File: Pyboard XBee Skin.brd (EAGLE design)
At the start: 33 x 26.9 mm, 8 parts

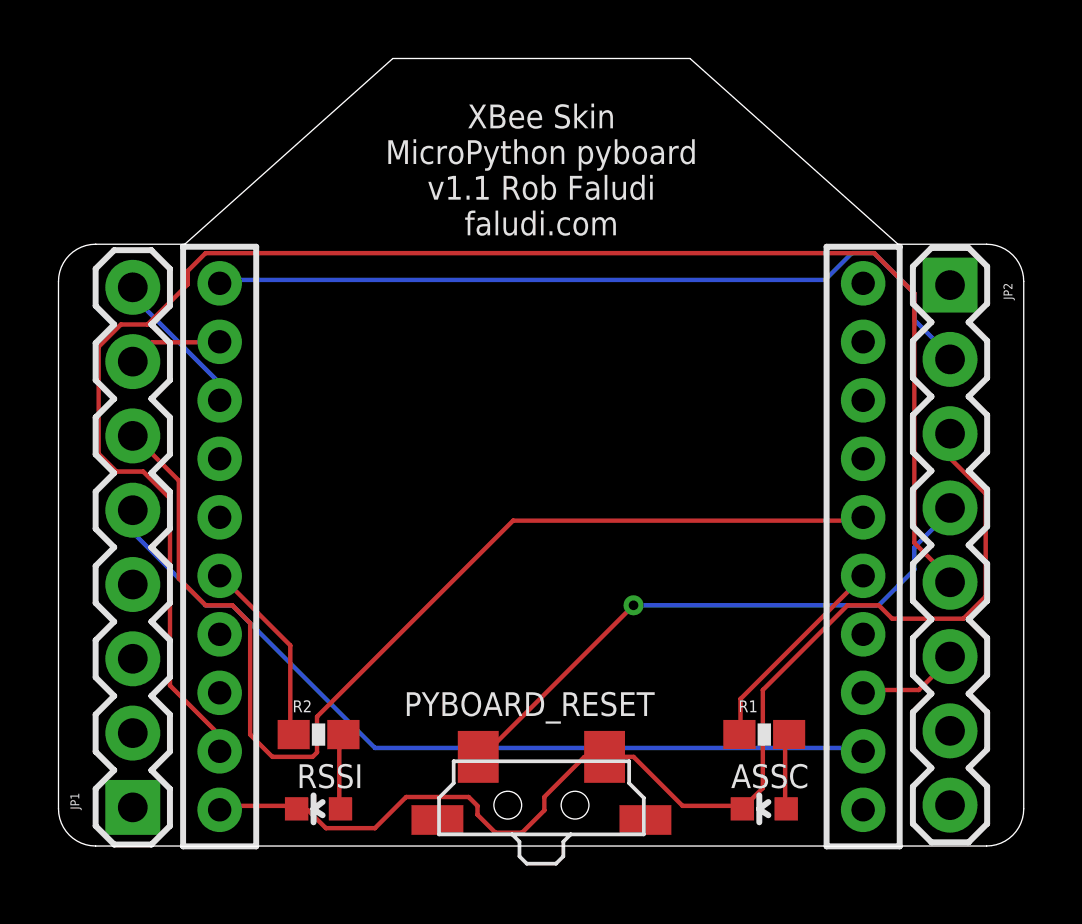
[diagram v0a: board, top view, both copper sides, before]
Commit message: Eagle CAD board design file v1.2
updates to silkscreen and reposition reset button
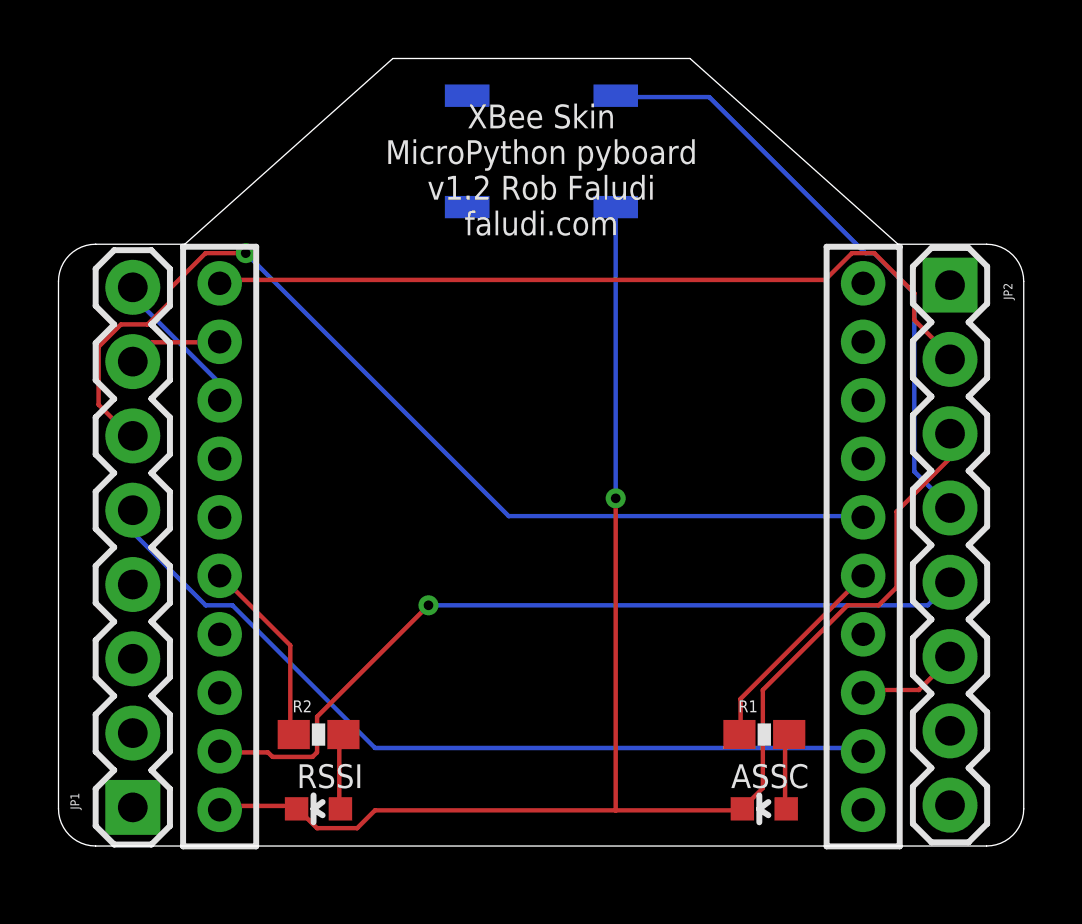
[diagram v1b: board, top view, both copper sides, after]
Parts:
- PYBOARD_RESET: device Seeed-OPL-Button:SW4-SMD-7.0X3.5X3.5MM-90D -> SparkFun-Electromechanical:TACTILE_SWITCH_SMD
- moved PYBOARD_RESET 22.4 mm to (16.5, 23.7), flipped to the bottom
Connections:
- net GND: now also PYBOARD_RESET.3; no longer PYBOARD_RESET.2
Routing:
- net SLP_CTRL: track 56.5 -> 28.2 mm, vias 0 -> 1
- net GND: track 41.2 -> 55.5 mm, vias 0 -> 1
- net RTS: track 37.8 -> 35.1 mm, vias 0 -> 1
- net RESET: track 20.2 -> 20.9 mm, vias 1 -> 0
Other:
- board text added: "XBee Skin MicroPython pyboard v1.2 Rob Faludi faludi.com"
- board text removed: "XBee Skin MicroPython pyboard v1.1 Rob Faludi faludi.com"
